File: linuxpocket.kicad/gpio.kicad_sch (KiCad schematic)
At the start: 15 parts, among them J1 XDSM-1035-08-KT, SW1 POWER, SW2 VOL_UP, SW3 VOL_DOWN, U9 LIS2MDL

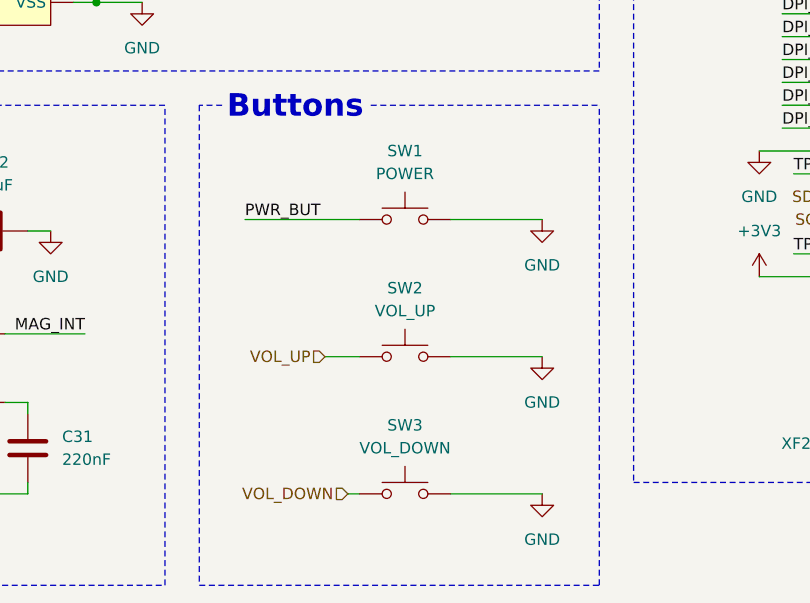
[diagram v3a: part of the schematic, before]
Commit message: Start placing components in PCB.
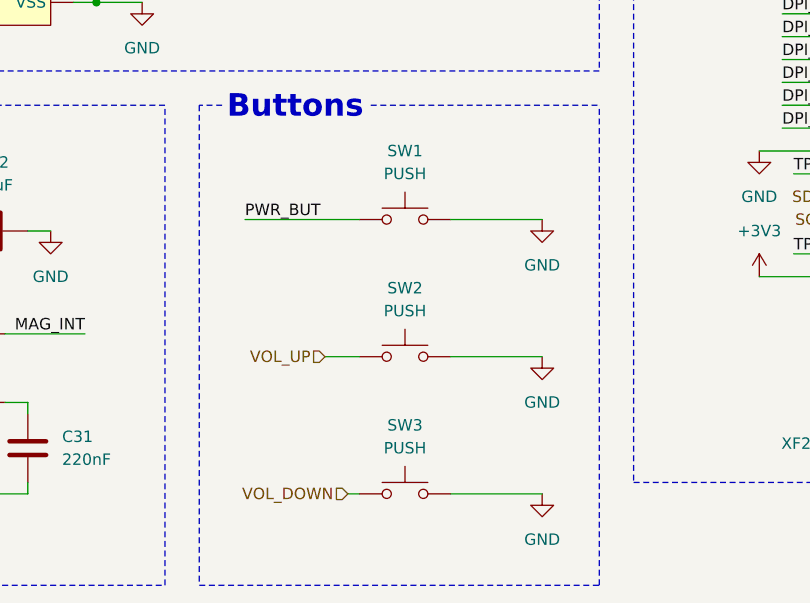
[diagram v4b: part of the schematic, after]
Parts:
- SW1: value POWER -> PUSH
- SW2: value VOL_UP -> PUSH
- SW3: value VOL_DOWN -> PUSH
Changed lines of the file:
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@@
 	(title_block
 		(title "GPIO and LowSpeed")
-		(date "2024-10-19")
+		(date "2024-10-19 - 2025-02-02")
 		(rev "Prototype v0")
 		(company "xamuel.xyz")
@@
 	)
 	(symbol
-		(lib_id "Switch:SW_Push")
-		(at 208.28 151.13 0)
-		(unit 1)
-		(exclude_from_sim no)
-		(in_bom yes)
-		(on_board yes)
-		(dnp no)
-		(fields_autoplaced yes)
-		(property "Reference" "SW3"
-			(at 208.28 143.51 0)
-			(effects
-				(font
-					(size 1.27 1.27)
-				)
-			)
-		)
-		(property "Value" "VOL_DOWN"
-			(at 208.28 146.05 0)
-			(effects
-				(font
-					(size 1.27 1.27)
-				)
-			)
-		)
-		(property "Footprint" "linuxpocket:SW-SMD_GT-TC020B-H035-L05"
-			(at 208.28 146.05 0)
-			(effects
-				(font
-					(size 1.27 1.27)
-				)
-				(hide yes)
-			)
-		)
-		(property "Datasheet" "~"
-			(at 208.28 146.05 0)
-			(effects
-				(font
-					(size 1.27 1.27)
-				)
-				(hide yes)
-			)
-		)
-		(property "Description" "Push button switch, generic, two pins"
-			(at 208.28 151.13 0)
-			(effects
-				(font
-					(size 1.27 1.27)
-				)
-				(hide yes)
-			)
-		)
-		(property "LCSC" "C17179534"
-			(at 208.28 151.13 0)
-			(effects
-				(font
-					(size 1.27 1.27)
-				)
-				(hide yes)
-			)
-		)
-		(pin "2"
-		)
-		(pin "1"
-		)
-		(instances
-			(project "linuxpocket"
-				(path "/de3771bf-b13a-459d-a957-6ff90f7da387/157d7587-4674-47d2-b2e3-79ed693e51a7"
-					(reference "SW3")
-					(unit 1)
-				)
-			)
-		)
-	)
-	(symbol
 		(lib_id "power:+1V8")
 		(at 25.4 130.81 0)
@@
 	)
 	(symbol
-		(lib_id "Switch:SW_Push")
-		(at 208.28 135.89 0)
-		(unit 1)
-		(exclude_from_sim no)
-		(in_bom yes)
-		(on_board yes)
-		(dnp no)
-		(fields_autoplaced yes)
-		(property "Reference" "SW2"
-			(at 208.28 128.27 0)
-			(effects
-				(font
-					(size 1.27 1.27)
-				)
-			)
-		)
-		(property "Value" "VOL_UP"
-			(at 208.28 130.81 0)
-			(effects
-				(font
-					(size 1.27 1.27)
-				)
-			)
-		)
-		(property "Footprint" "linuxpocket:SW-SMD_GT-TC020B-H035-L05"
-			(at 208.28 130.81 0)
-			(effects
-				(font
-					(size 1.27 1.27)
-				)
-				(hide yes)
-			)
-		)
-		(property "Datasheet" "~"
-			(at 208.28 130.81 0)
-			(effects
-				(font
-					(size 1.27 1.27)
-				)
-				(hide yes)
-			)
-		)
-		(property "Description" "Push button switch, generic, two pins"
-			(at 208.28 135.89 0)
-			(effects
-				(font
-					(size 1.27 1.27)
-				)
-				(hide yes)
-			)
-		)
-		(property "LCSC" "C17179534"
-			(at 208.28 135.89 0)
-			(effects
-				(font
-					(size 1.27 1.27)
-				)
-				(hide yes)
-			)
-		)
-		(pin "2"
-		)
-		(pin "1"
-		)
-		(instances
-			(project "linuxpocket"
-				(path "/de3771bf-b13a-459d-a957-6ff90f7da387/157d7587-4674-47d2-b2e3-79ed693e51a7"
-					(reference "SW2")
-					(unit 1)
-				)
-			)
-		)
-	)
-	(symbol
 		(lib_id "power:GND")
 		(at 179.07 96.52 0)
@@
 			)
 		)
-		(property "Value" "POWER"
+		(property "Value" "PUSH"
 			(at 208.28 115.57 0)
 			(effects
@@
 	)
 	(symbol
+		(lib_id "Switch:SW_Push")
+		(at 208.28 135.89 0)
+		(unit 1)
+		(exclude_from_sim no)
+		(in_bom yes)
+		(on_board yes)
+		(dnp no)
+		(fields_autoplaced yes)
+		(property "Reference" "SW2"
+			(at 208.28 128.27 0)
+			(effects
+				(font
+					(size 1.27 1.27)
+				)
+			)
+		)
+		(property "Value" "PUSH"
+			(at 208.28 130.81 0)
+			(effects
+				(font
+					(size 1.27 1.27)
+				)
+			)
+		)
+		(property "Footprint" "linuxpocket:SW-SMD_GT-TC020B-H035-L05"
+			(at 208.28 130.81 0)
+			(effects
+				(font
+					(size 1.27 1.27)
+				)
+				(hide yes)
+			)
+		)
+		(property "Datasheet" "~"
+			(at 208.28 130.81 0)
+			(effects
+				(font
+					(size 1.27 1.27)
+				)
+				(hide yes)
+			)
+		)
+		(property "Description" "Push button switch, generic, two pins"
+			(at 208.28 135.89 0)
+			(effects
+				(font
+					(size 1.27 1.27)
+				)
+				(hide yes)
+			)
+		)
+		(property "LCSC" "C17179534"
+			(at 208.28 135.89 0)
+			(effects
+				(font
+					(size 1.27 1.27)
+				)
+				(hide yes)
+			)
+		)
+		(pin "2"
+		)
+		(pin "1"
+		)
+		(instances
+			(project "linuxpocket"
+				(path "/de3771bf-b13a-459d-a957-6ff90f7da387/157d7587-4674-47d2-b2e3-79ed693e51a7"
+					(reference "SW2")
+					(unit 1)
+				)
+			)
+		)
+	)
+	(symbol
 		(lib_id "power:GND")
 		(at 259.08 35.56 0)
@@
 					(unit 1)
 				)
+			)
+		)
+	)
+	(symbol
+		(lib_id "Switch:SW_Push")
+		(at 208.28 151.13 0)
+		(unit 1)
+		(exclude_from_sim no)
+		(in_bom yes)
+		(on_board yes)
+		(dnp no)
+		(fields_autoplaced yes)
+		(property "Reference" "SW3"
+			(at 208.28 143.51 0)
+			(effects
+				(font
+					(size 1.27 1.27)
+				)
+			)
+		)
+		(property "Value" "PUSH"
+			(at 208.28 146.05 0)
+			(effects
+				(font
+					(size 1.27 1.27)
+				)
+			)
+		)
+		(property "Footprint" "linuxpocket:SW-SMD_GT-TC020B-H035-L05"
+			(at 208.28 146.05 0)
+			(effects
+				(font
+					(size 1.27 1.27)
+				)
+				(hide yes)
+			)
+		)
+		(property "Datasheet" "~"
+			(at 208.28 146.05 0)
+			(effects
+				(font
+					(size 1.27 1.27)
+				)
+				(hide yes)
+			)
+		)
+		(property "Description" "Push button switch, generic, two pins"
+			(at 208.28 151.13 0)
+			(effects
+				(font
+					(size 1.27 1.27)
+				)
+				(hide yes)
+			)
+		)
+		(property "LCSC" "C17179534"
+			(at 208.28 151.13 0)
+			(effects
+				(font
+					(size 1.27 1.27)
+				)
+				(hide yes)
+			)
+		)
+		(pin "2"
+		)
+		(pin "1"
+		)
+		(instances
+			(project "linuxpocket"
+				(path "/de3771bf-b13a-459d-a957-6ff90f7da387/157d7587-4674-47d2-b2e3-79ed693e51a7"
+					(reference "SW3")
+					(unit 1)
+				)

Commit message: PCB almost done and schematic finished.
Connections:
- net MAG_INT: now also Module1.47 (GPIO23)
- net USB-INT renamed RI
- no-connect marks 26 -> 27
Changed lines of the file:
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@@
 	)
 	(no_connect
+		(at 250.19 41.91)
+	)
+	(no_connect
 		(at 36.83 41.91)
 	)
@@
 	(wire
 		(pts
-			(xy 97.79 77.47) (xy 101.6 77.47)
+			(xy 101.6 77.47) (xy 101.6 76.2)
 		)
 		(stroke
@@
 	(wire
 		(pts
-			(xy 97.79 72.39) (xy 102.87 72.39)
+			(xy 97.79 72.39) (xy 109.22 72.39)
 		)
 		(stroke
@@
 	(wire
 		(pts
+			(xy 97.79 80.01) (xy 113.03 80.01)
+		)
+		(stroke
+			(width 0)
+			(type default)
+		)
+	)
+	(wire
+		(pts
 			(xy 173.99 68.58) (xy 173.99 71.12)
 		)
@@
 	(wire
 		(pts
+			(xy 100.33 74.93) (xy 100.33 87.63)
+		)
+		(stroke
+			(width 0)
+			(type default)
+			(color 0 0 0 1)
+		)
+	)
+	(wire
+		(pts
 			(xy 209.55 25.4) (xy 217.17 25.4)
 		)
@@
 	(wire
 		(pts
-			(xy 100.33 74.93) (xy 100.33 87.63)
-		)
-		(stroke
-			(width 0)
-			(type default)
-			(color 0 0 0 1)
-		)
-	)
-	(wire
-		(pts
 			(xy 134.62 135.89) (xy 138.43 135.89)
 		)
@@
 	(wire
 		(pts
+			(xy 97.79 77.47) (xy 101.6 77.47)
+		)
+		(stroke
+			(width 0)
+			(type default)
+		)
+	)
+	(wire
+		(pts
 			(xy 21.59 135.89) (xy 36.83 135.89)
 		)
@@
 		)
 	)
+	(label "MAG_INT"
+		(at 113.03 80.01 180)
+		(fields_autoplaced yes)
+		(effects
+			(font
+				(size 1.27 1.27)
+				(thickness 0.1588)
+			)
+			(justify right bottom)
+		)
+	)
 	(label "DPI_D8"
 		(at 250.19 87.63 0)
@@
 	(hierarchical_label "GAUGE_INT"
 		(shape input)
-		(at 101.6 77.47 0)
+		(at 101.6 76.2 0)
 		(fields_autoplaced yes)
 		(effects
@@
 		)
 	)
-	(hierarchical_label "USB-INT"
+	(hierarchical_label "RI"
 		(shape input)
-		(at 102.87 72.39 0)
+		(at 109.22 72.39 0)
 		(fields_autoplaced yes)
 		(effects

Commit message: PCB basically finished.
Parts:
- Module1: LCSC C424649 -> C19089325
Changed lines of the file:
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@@
 			)
 		)
-		(property "LCSC" "C424649"
+		(property "LCSC" "C19089325"
 			(at 69.85 77.47 0)
 			(effects
